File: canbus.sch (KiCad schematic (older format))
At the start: 17 parts, among them J601 Conn_01x04, J602 Conn_01x02, U601 RCLAMP0524P-N, U602 ISO1050DUB, U603 H7550-H#

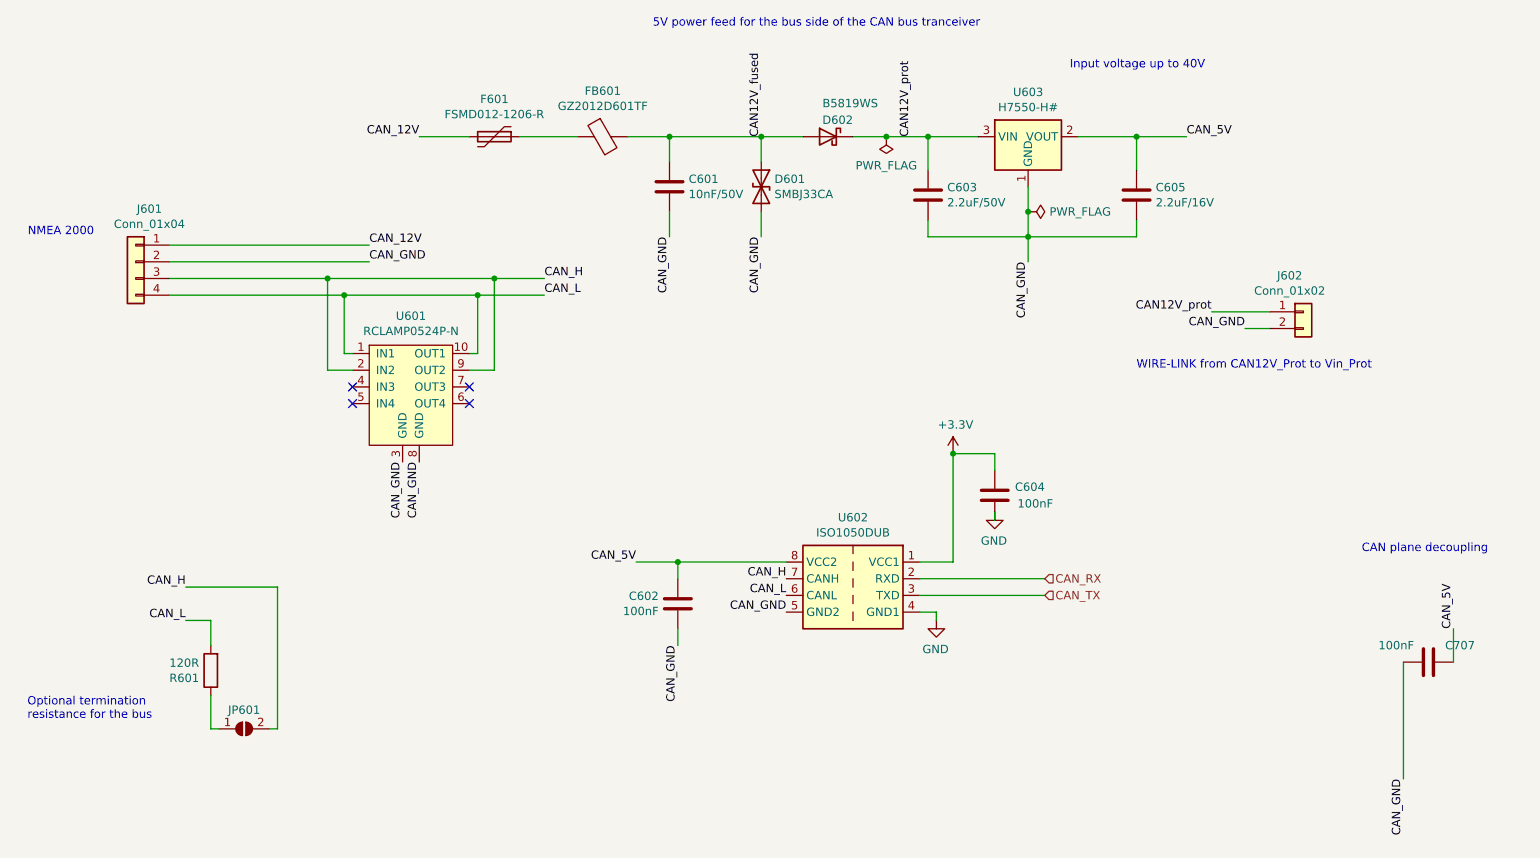
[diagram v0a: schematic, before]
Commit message: Swap D602 to B5819W which is a standard component
Due to the larger footprint, some layout changes were required.
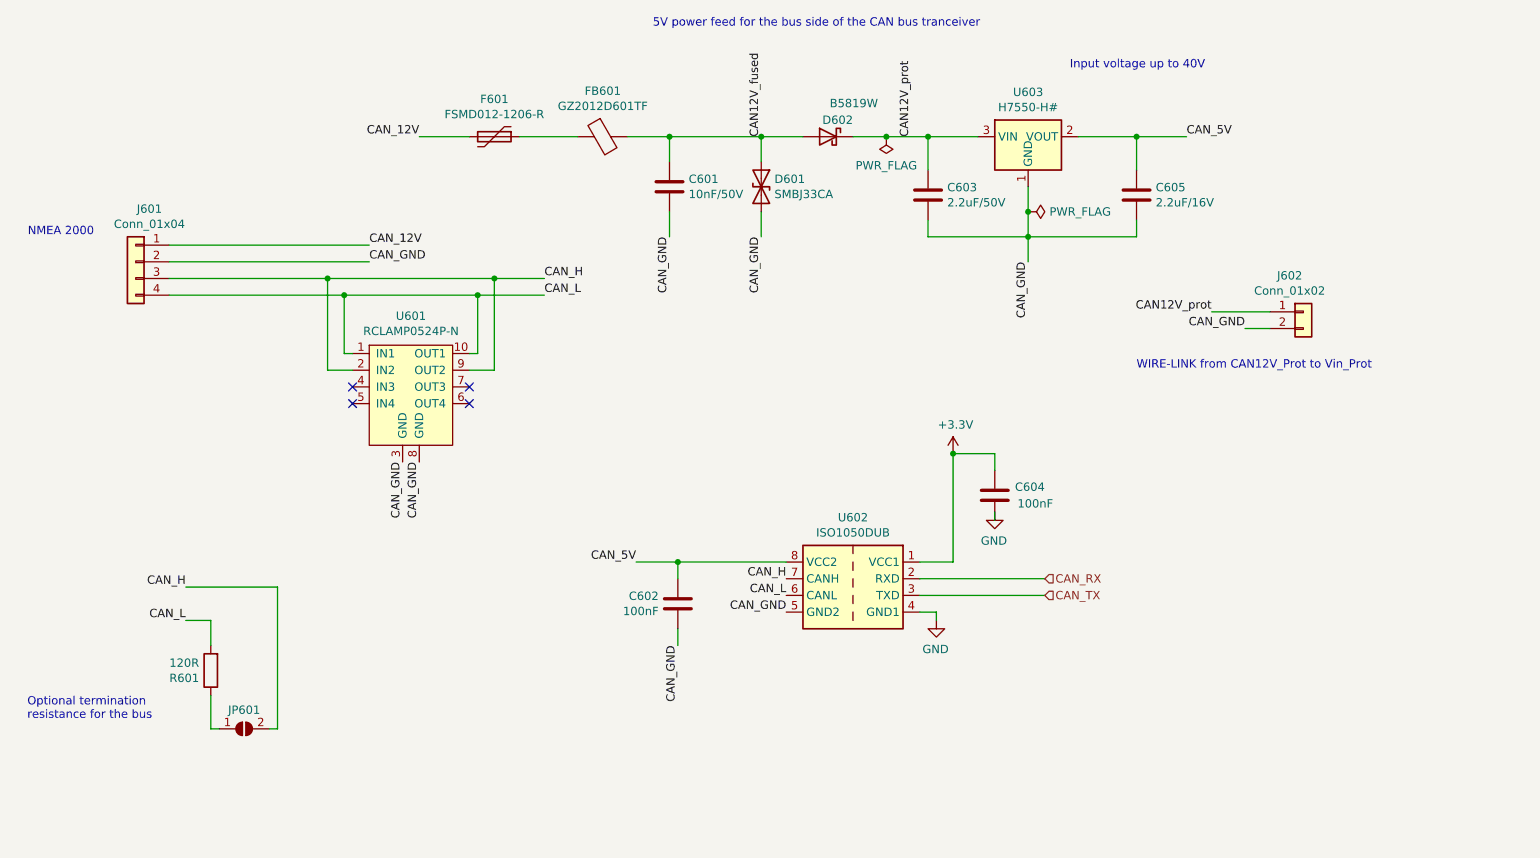
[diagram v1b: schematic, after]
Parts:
- removed C707: 100nF, Capacitor_SMD:C_0402_1005Metric, symbol Device:C
- D602: value B5819WS -> B5819W; footprint Diode_SMD:D_SOD-323F -> Diode_SMD:D_SOD-123; LCSC C123899 -> C8598
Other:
- note removed: "CAN plane decoupling"
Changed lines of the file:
@@
 $Descr A4 11693 8268
 encoding utf-8
-Sheet 7 11
+Sheet 6 11
 Title "Sailor Hat for ESP32"
 Date "2020-11-25"
@@
 AR Path="/5F733BA4/5FB60F25" Ref="D602"  Part="1"
 F 0 "D602" H 5650 1550 50  0000 L CNN
-F 1 "B5819WS" H 5500 1650 50  0000 L CNN
-F 2 "Diode_SMD:D_SOD-323F" H 5800 1450 50  0001 C CNN
+F 1 "B5819W" H 5500 1650 50  0000 L CNN
+F 2 "Diode_SMD:D_SOD-123" H 5800 1450 50  0001 C CNN
 F 3 "~" H 5800 1450 50  0001 C CNN
 F 4 "" V 5800 1450 50  0001 C CNN "Notes"
-F 5 "C123899" H 5800 1450 50  0001 C CNN "LCSC"
+F 5 "C8598" H 5800 1450 50  0001 C CNN "LCSC"
 	1    5800 1450
 	-1   0    0    -1
@@
 Wire Wire Line
 	2450 5000 2500 5000
-$Comp
-L Device:C C?
-U 1 1 5FB9BEFB
-P 9400 4600
-AR Path="/5D6F1C7C/5FB9BEFB" Ref="C?"  Part="1"
-AR Path="/5C348474/5FB9BEFB" Ref="C?"  Part="1"
-AR Path="/5F733BA4/5FB9BEFB" Ref="C707"  Part="1"
-F 0 "C707" V 9500 4700 50  0000 L CNN
-F 1 "100nF" V 9500 4300 50  0000 L CNN
-F 2 "Capacitor_SMD:C_0402_1005Metric" H 9438 4450 50  0001 C CNN
-F 3 "~" H 9400 4600 50  0001 C CNN
-F 4 "C1525" H 9400 4600 50  0001 C CNN "LCSC"
-	1    9400 4600
-	0    1    -1   0
-$EndComp
-Text Label 9250 5300 3    50   ~ 0
-CAN_GND
-Text Label 9550 4400 1    50   ~ 0
-CAN_5V
-Wire Wire Line
-	9550 4400 9550 4600
-Wire Wire Line
-	9250 4600 9250 5300
-Text Notes 9000 3950 0    50   ~ 0
-CAN plane decoupling
 $EndSCHEMATC

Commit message: Fix C603 part number to match the footprint
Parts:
- C603: LCSC C50254 -> C49217
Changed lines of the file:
@@
 F 2 "Capacitor_SMD:C_0805_2012Metric" H 6438 1650 50  0001 C CNN
 F 3 "~" H 6400 1800 50  0001 C CNN
-F 4 "C50254" H 6400 1800 50  0001 C CNN "LCSC"
+F 4 "C49217" H 6400 1800 50  0001 C CNN "LCSC"
 	1    6400 1800
 	1    0    0    -1

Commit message: Switch power and  NEMA to JST-XH Connectors and update silkscreen accordingly
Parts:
- J601: footprint Connector_Phoenix_MC:PhoenixContact_MCV_1,5_4-G-3.81_1x04_P3.81mm_Vertical -> Connector_JST:JST_XH_B4B-XH-A_1x04_P2.50mm_Vertical
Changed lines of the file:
@@
 F 0 "J601" H 1568 2517 50  0000 C CNN
 F 1 "Conn_01x04" H 1568 2426 50  0000 C CNN
-F 2 "Connector_Phoenix_MC:PhoenixContact_MCV_1,5_4-G-3.81_1x04_P3.81mm_Vertical" H 1650 2200 50  0001 C CNN
+F 2 "Connector_JST:JST_XH_B4B-XH-A_1x04_P2.50mm_Vertical" H 1650 2200 50  0001 C CNN
 F 3 "~" H 1650 2200 50  0001 C CNN
 F 4 "C8410" H 1650 2200 50  0001 C CNN "LCSC"

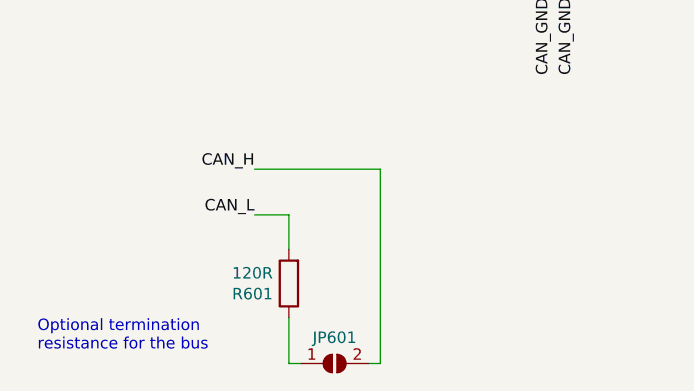
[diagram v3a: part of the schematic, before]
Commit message: Increase thermal clearances of copper fills to improve solderability
Also swapped the 120R 1206 termination resistor to two 240R 0805
resistors due to JLCPCB basic catalog availability.
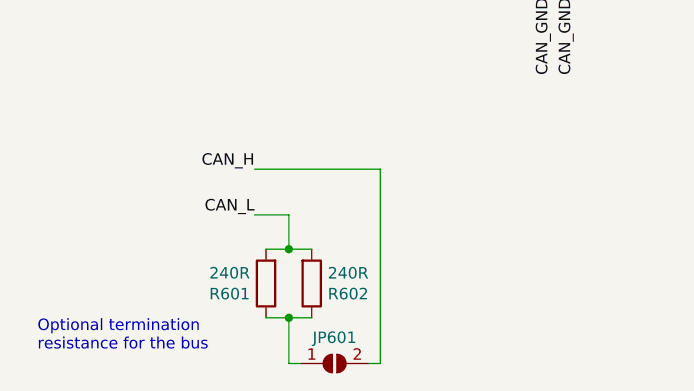
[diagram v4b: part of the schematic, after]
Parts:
- added R602: 240R, Resistor_SMD:R_0805_2012Metric, symbol Device:R
- R601: value 120R -> 240R; footprint Resistor_SMD:R_1206_3216Metric -> Resistor_SMD:R_0805_2012Metric; LCSC C17909 -> C17572; Notes Min 0.25W -> (none)
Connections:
- net CAN_L: now also R602.2
- net at JP601.1 (A), R601.1: now also R602.1
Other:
- moved on the sheet: R601
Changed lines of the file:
@@
 L Device:R R601
 U 1 1 5C353BFC
-P 2100 4650
-F 0 "R601" H 2170 4696 50  0000 L CNN
-F 1 "120R" H 2170 4605 50  0000 L CNN
-F 2 "Resistor_SMD:R_1206_3216Metric" V 2030 4650 50  0001 C CNN
-F 3 "~" H 2100 4650 50  0001 C CNN
-F 4 "" H 2100 4650 50  0001 C CNN "Note"
-F 5 "Min 0.25W" H -5000 3100 50  0001 C CNN "Notes"
-F 6 "C17909" H 2100 4650 50  0001 C CNN "LCSC"
-	1    2100 4650
+P 2000 4650
+F 0 "R601" H 2070 4696 50  0000 L CNN
+F 1 "240R" H 2070 4605 50  0000 L CNN
+F 2 "Resistor_SMD:R_0805_2012Metric" V 1930 4650 50  0001 C CNN
+F 3 "~" H 2000 4650 50  0001 C CNN
+F 4 "" H 2000 4650 50  0001 C CNN "Note"
+F 5 "" H -5100 3100 50  0001 C CNN "Notes"
+F 6 "C17572" H 2000 4650 50  0001 C CNN "LCSC"
+	1    2000 4650
 	-1   0    0    1
 $EndComp
@@
 Wire Wire Line
 	2450 5000 2500 5000
+$Comp
+L Device:R R602
+U 1 1 5FE01F73
+P 2200 4650
+F 0 "R602" H 2270 4696 50  0000 L CNN
+F 1 "240R" H 2270 4605 50  0000 L CNN
+F 2 "Resistor_SMD:R_0805_2012Metric" V 2130 4650 50  0001 C CNN
+F 3 "~" H 2200 4650 50  0001 C CNN
+F 4 "" H 2200 4650 50  0001 C CNN "Note"
+F 5 "" H -4900 3100 50  0001 C CNN "Notes"
+F 6 "C17572" H 2200 4650 50  0001 C CNN "LCSC"
+	1    2200 4650
+	1    0    0    1
+$EndComp
+Wire Wire Line
+	2000 4800 2100 4800
+Connection ~ 2100 4800
+Wire Wire Line
+	2100 4800 2200 4800
+Wire Wire Line
+	2000 4500 2100 4500
+Connection ~ 2100 4500
+Wire Wire Line
+	2100 4500 2200 4500
 $EndSCHEMATC

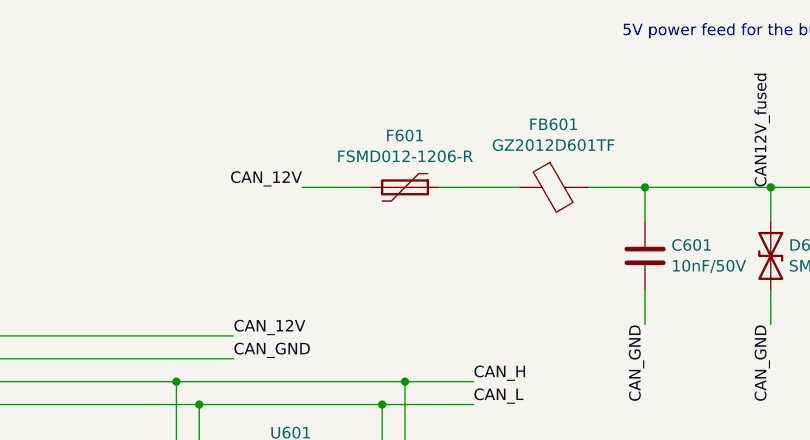
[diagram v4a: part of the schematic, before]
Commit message: Power system bug fix. Changed fuses & Diode - Swapping incorrect part  D1101 and D1102  to BAT54A   /  LCSC:  C83936 -Removed Perfect Diode, replaced with B5819W  Schottky - Replaced USB PTC Fuse ( F401 ) with   ASMD1206-050  /   C135338 - Replaced VIN ( F301 ) & CAN (F601 )PTC Fuses with  mSMD050-60V  / C70113 - Rerouted power and CAN power areas of board. - Removed all perfectDiode components/tracks and replaced with Schottky
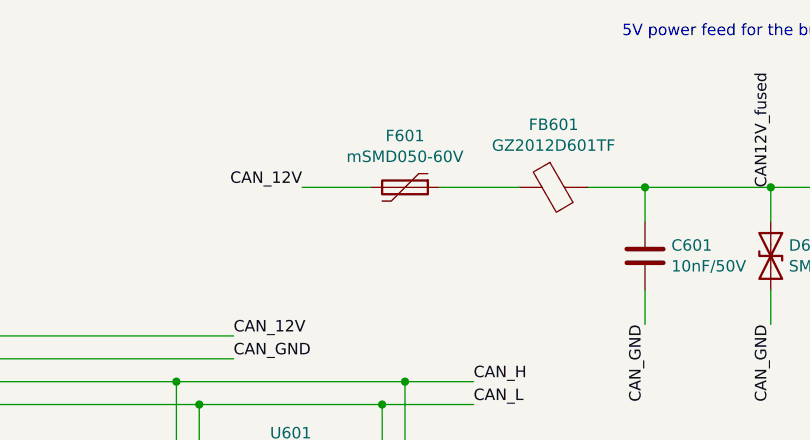
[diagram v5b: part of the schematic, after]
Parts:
- F601: value FSMD012-1206-R -> mSMD050-60V; footprint Fuse:Fuse_1206_3216Metric -> Fuse:Fuse_1812_4532Metric; LCSC C220144 -> C70113
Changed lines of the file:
@@
 $Descr A4 11693 8268
 encoding utf-8
-Sheet 6 11
+Sheet 5 10
 Title "Sailor Hat for ESP32"
 Date "2020-11-25"
@@
 AR Path="/5F733BA4/5F94C963" Ref="F601"  Part="1"
 F 0 "F601" V 3575 1450 50  0000 C CNN
-F 1 "FSMD012-1206-R" V 3666 1450 50  0000 C CNN
-F 2 "Fuse:Fuse_1206_3216Metric" H 3850 1250 50  0001 L CNN
-F 3 "~" H 3800 1450 50  0001 C CNN
-F 4 "C220144" H 3800 1450 50  0001 C CNN "LCSC"
+F 1 "mSMD050-60V" V 3666 1450 50  0000 C CNN
+F 2 "Fuse:Fuse_1812_4532Metric" H 3850 1250 50  0001 L CNN
+F 3 "https://datasheet.lcsc.com/szlcsc/TECHFUSE-mSMD050-60V_C70113.pdf" H 3800 1450 50  0001 C CNN
+F 4 "C70113" H 3800 1450 50  0001 C CNN "LCSC"
 	1    3800 1450
 	0    1    1    0

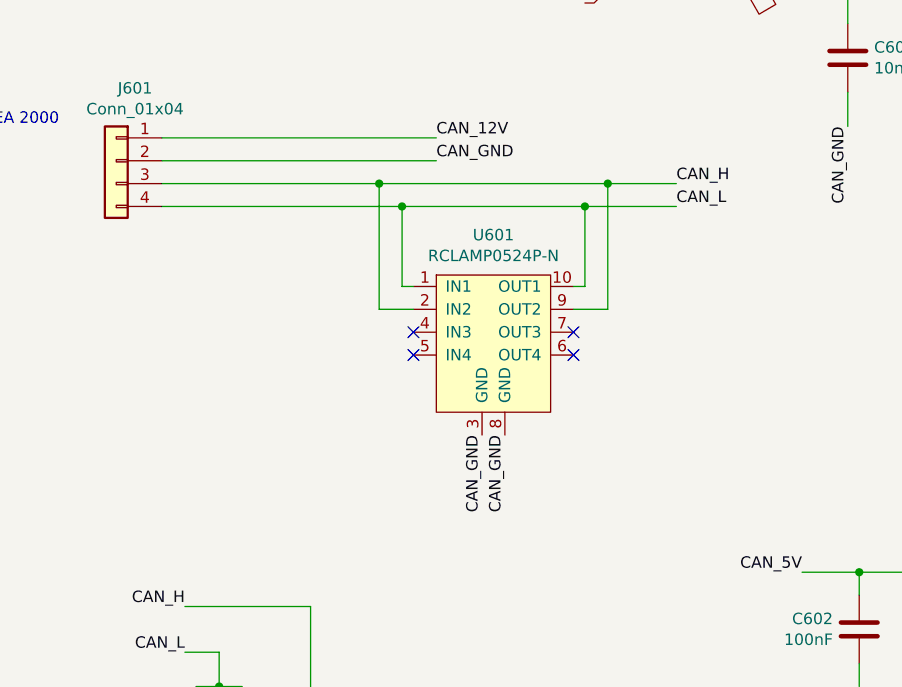
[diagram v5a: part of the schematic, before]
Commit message: Remove RClamp on CAN bus input
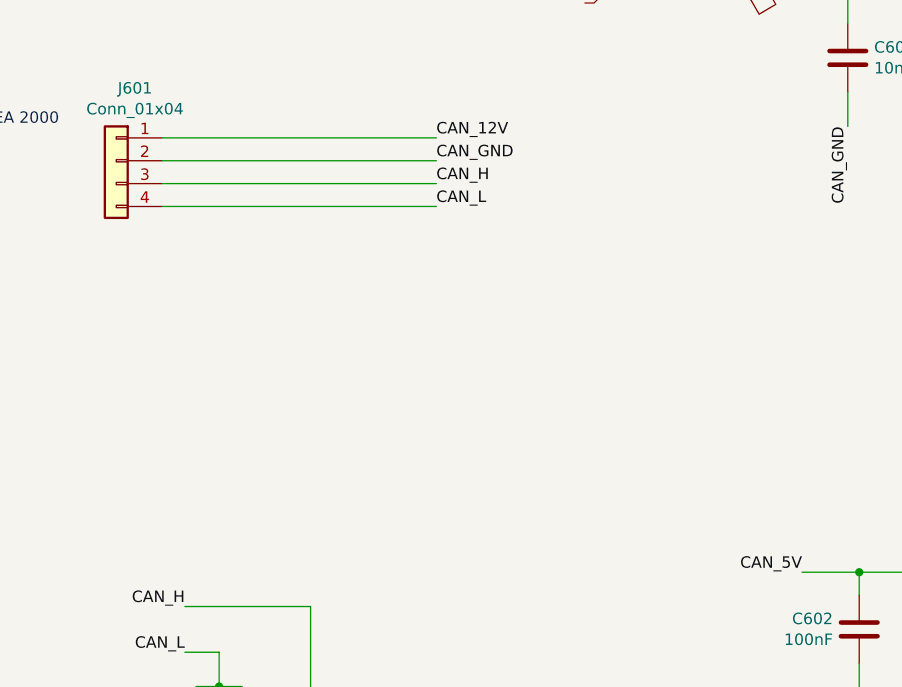
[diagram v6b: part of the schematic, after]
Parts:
- removed U601: RCLAMP0524P-N, Package_DFN_QFN:Diodes_UDFN-10_1.0x2.5mm_P0.5mm, symbol SH-ESP32:RCLAMP0524P-N
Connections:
- no-connect marks 4 -> 0
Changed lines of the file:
@@
 Text Label 3050 2100 0    50   ~ 0
 CAN_12V
-Text Label 4100 2400 0    50   ~ 0
+Text Label 3050 2400 0    50   ~ 0
 CAN_L
-Text Label 4100 2300 0    50   ~ 0
+Text Label 3050 2300 0    50   ~ 0
 CAN_H
 Text Label 4900 4500 3    50   ~ 0
@@
 $EndComp
 $Comp
-L SH-ESP32:RCLAMP0524P-N U601
-U 1 1 5FBB6763
-P 3300 2950
-F 0 "U601" H 3300 3375 50  0000 C CNN
-F 1 "RCLAMP0524P-N" H 3300 3284 50  0000 C CNN
-F 2 "Package_DFN_QFN:Diodes_UDFN-10_1.0x2.5mm_P0.5mm" H 3300 2850 50  0001 C CNN
-F 3 "" H 3300 2850 50  0001 C CNN
-F 4 "C316044" H 3300 2950 50  0001 C CNN "LCSC"
-	1    3300 2950
-	1    0    0    -1
-$EndComp
-NoConn ~ 2950 2950
-NoConn ~ 2950 3050
-NoConn ~ 3650 2950
-NoConn ~ 3650 3050
-Text Label 3250 3400 3    50   ~ 0
-CAN_GND
-Text Label 3350 3400 3    50   ~ 0
-CAN_GND
-$Comp
 L Device:C C?
 U 1 1 5FBC67EE
@@
 	-1   0    0    -1
 $EndComp
-Wire Wire Line
-	1850 2300 2800 2300
-Wire Wire Line
-	1850 2400 2900 2400
-Wire Wire Line
-	2950 2750 2900 2750
-Wire Wire Line
-	2900 2750 2900 2400
-Connection ~ 2900 2400
-Wire Wire Line
-	2900 2400 3700 2400
-Wire Wire Line
-	3650 2750 3700 2750
-Wire Wire Line
-	3700 2750 3700 2400
-Connection ~ 3700 2400
-Wire Wire Line
-	3700 2400 4100 2400
-Wire Wire Line
-	2950 2850 2800 2850
-Wire Wire Line
-	2800 2850 2800 2300
-Connection ~ 2800 2300
-Wire Wire Line
-	2800 2300 3800 2300
-Wire Wire Line
-	3650 2850 3800 2850
-Wire Wire Line
-	3800 2850 3800 2300
-Connection ~ 3800 2300
-Wire Wire Line
-	3800 2300 4100 2300
 Text Notes 7250 1050 0    50   ~ 0
 Input voltage up to 40V
@@
 Wire Wire Line
 	2100 4500 2200 4500
+Wire Wire Line
+	1850 2300 3050 2300
+Wire Wire Line
+	1850 2400 3050 2400
 $EndSCHEMATC
